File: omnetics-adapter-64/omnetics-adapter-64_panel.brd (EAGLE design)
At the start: 109 x 119 mm, 255 parts, among them J1 DF40-REC, J10 DF40-REC, J13 DF40-REC, J16 DF40-REC, J17 DF40-REC, J22 DF40-REC, J25 DF40-REC, J28 DF40-REC, J31 DF40-REC, J34 DF40-REC, J37 DF40-REC, J4 DF40-REC, J40 DF40-REC, J43 DF40-REC, J46 DF40-REC, J49 DF40-REC, J52 DF40-REC, J55 DF40-REC, J58 DF40-REC, J61 DF40-REC, J64 DF40-REC, J67 DF40-REC, J7 DF40-REC, J70 DF40-REC, J73 DF40-REC, J76 DF40-REC, J79 DF40-REC, J82 DF40-REC

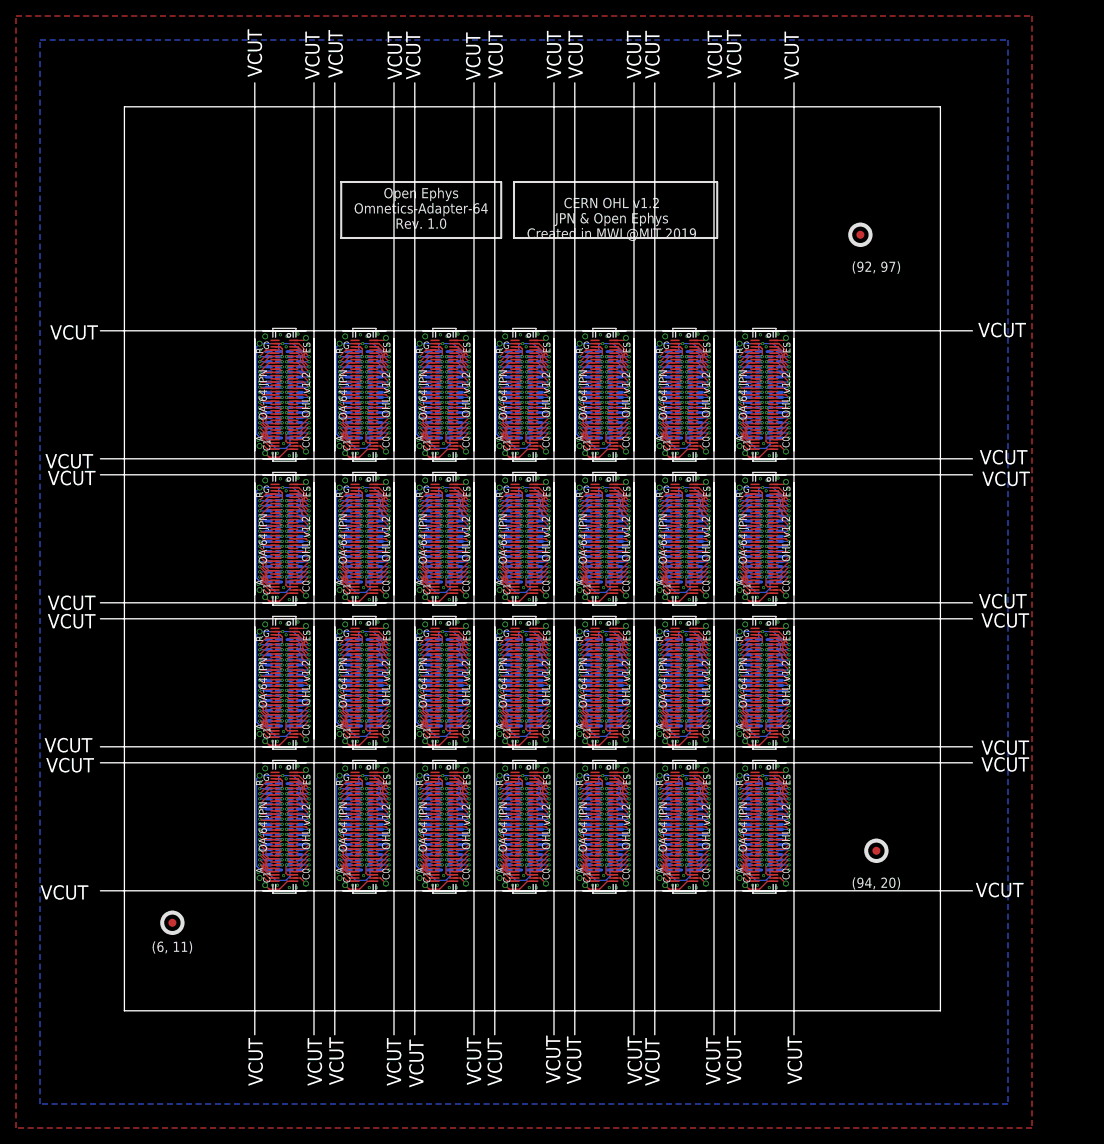
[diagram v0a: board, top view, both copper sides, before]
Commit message: Update omnetics-adapter-64 with Filipe's suggestions
- The suggestions addressed are as follows:
- Increase alls pads of J1 by at least 0.5 mm to the exterior. I believe
this board will be completely assembled by hand and this facilitates
assembly and shorts removal.
- Have 2 mm from the tip of the Omnetics pad to the outline of the
board. This gives us room to apply the necessary epoxy.
- Add some 0.3 holes around the Omnetics to help to fix the epoxy.
- Reduce a little bit the roundness of the Omnetics pads, but not
completely. I would say to half of the current roundness.
- Move the silk indications away from the epoxy application and the
extension of the J1 pads. (done in the board i'm sending)
- Can we write Open-Ephys somewhere in the top silk?
- In the panel, Vcut only for the sides of the board parallel to the
connectors. Milling in the rest. Easier to detach due to J1 being
outside the board boundaries.
- In the panel, a distance between board center to board center of 25 mm
is suggested. (I'm sending the current panel for reference)
- In the panel, if the non-90degrees individual board's corner can
prevail, it would be better: it's more elegant and to grab-friendly.
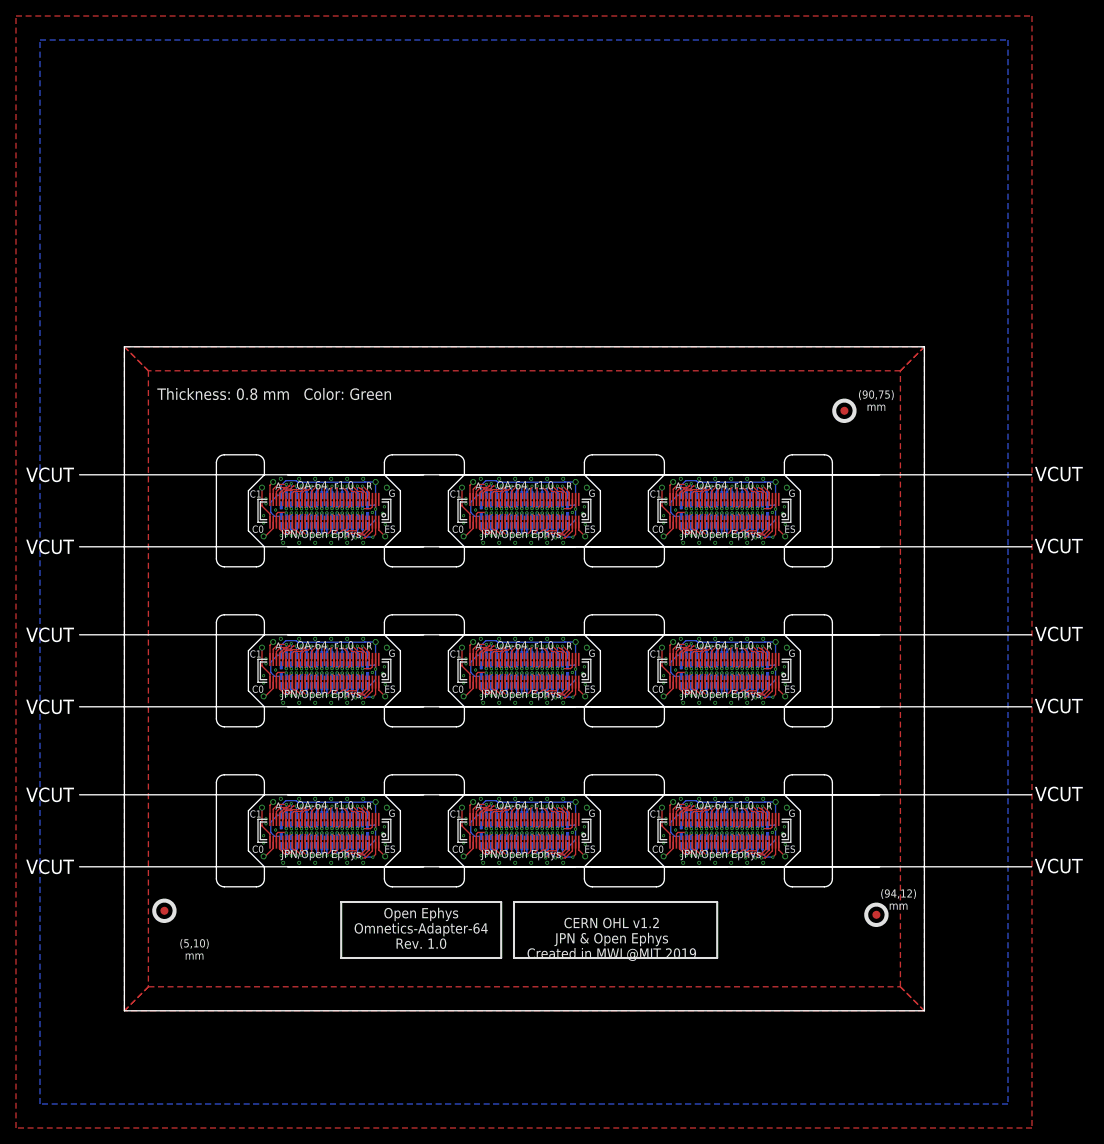
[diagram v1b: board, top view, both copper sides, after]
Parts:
- removed AN10, AN11, AN12, AN13, AN14, AN15, AN16, AN17, AN18, AN19, AN20, AN21, AN22, AN23, AN24, AN25, AN26, AN27, AN28, AN9, CAT18, CAT19, CAT20, CAT21, CAT22, CAT23, CAT24, CAT25, CAT26, CAT27, CAT28, CAT29, CAT30, CAT31, CAT32, CAT33, CAT34, CAT35, CAT36, CAT37, CAT38, CAT39, CAT40, CAT41, CAT42, CAT43, CAT44, CAT45, CAT46, CAT47, CAT48, CAT49, CAT50, CAT51, CAT52, CAT53, CAT54, CAT55, CAT56, ESTIM27, ESTIM28, ESTIM29, ESTIM30, ESTIM31, ESTIM32, ESTIM33, ESTIM34, ESTIM35, ESTIM36, ESTIM37, ESTIM38, ESTIM39, ESTIM40, ESTIM41, ESTIM42, ESTIM43, ESTIM44, ESTIM45, ESTIM46, ESTIM47, ESTIM48, ESTIM49, ESTIM50, ESTIM51, ESTIM52, ESTIM53, ESTIM54, ESTIM55, ESTIM56, ESTIM57, ESTIM58, ESTIM59, ESTIM60, ESTIM61, ESTIM62, ESTIM63, ESTIM64, ESTIM65, ESTIM66, ESTIM67, ESTIM68, ESTIM69, ESTIM70, ESTIM71, ESTIM72, ESTIM73, ESTIM74, ESTIM75, ESTIM76, ESTIM77, ESTIM78, ESTIM79, ESTIM80, ESTIM81, ESTIM82, ESTIM83, ESTIM84: LRG_GP, jonnew:GOLDPIN_0.5ID_0.7OD
- removed E$4: (no value), fiducial:FIDUCIAL
- removed J28, J31, J34, J37, J40, J43, J46, J49, J52, J55, J58, J61, J64, J67, J70, J73, J76, J79, J82: DF40-REC, jonnew:DF40-70REC
- removed J29, J30, J32, J33, J35, J36, J38, J39, J41, J42, J44, J45, J47, J48, J50, J51, J53, J54, J56, J57, J59, J60, J62, J63, J65, J66, J68, J69, J71, J72, J74, J75, J77, J78, J80, J81, J83, J84: (no value), jonnew:NPD-36-VV-GS
- added AN, CAT0, ESTIM: LRG_GP, jonnew:GOLDPIN_0.5ID_0.7OD
- added E$3: (no value), fiducial:FIDUCIAL
- J1, J10, J13, J16, J22, J25, J4, J7: device jonnew:DF40-70REC -> jonnew:DDF40-70REC-LRG
- J17: value DF40-REC -> (none); device jonnew:DF40-70REC -> jonnew:NPD-36-VV-GS
- J19: value (none) -> DF40-REC; device jonnew:NPD-36-VV-GS -> jonnew:DDF40-70REC-LRG
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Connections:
- removed net AN10: AN10.P$1, J31.36
- removed net AN11: AN11.P$1, J34.36
- removed net AN12: AN12.P$1, J37.36
- removed net AN13: AN13.P$1, J40.36
- removed net AN14: AN14.P$1, J43.36
- removed net AN15: AN15.P$1, J46.36
- removed net AN16: AN16.P$1, J17.36
- removed net AN17: AN17.P$1, J49.36
- removed net AN18: AN18.P$1, J52.36
- removed net AN19: AN19.P$1, J55.36
- removed net AN20: AN20.P$1, J58.36
- removed net AN21: AN21.P$1, J61.36
- removed net AN22: AN22.P$1, J64.36
- removed net AN23: AN23.P$1, J67.36
- removed net AN24: AN24.P$1, J70.36
- removed net AN25: AN25.P$1, J73.36
- removed net AN26: AN26.P$1, J76.36
- removed net AN27: AN27.P$1, J79.36
- removed net AN28: AN28.P$1, J82.36
- removed net AN9: AN9.P$1, J28.36
- removed net CAT18: CAT18.P$1, J28.35
- removed net CAT19: CAT19.P$1, J31.34
- removed net CAT20: CAT20.P$1, J31.35
- removed net CAT21: CAT21.P$1, J34.34
- removed net CAT22: CAT22.P$1, J34.35
- removed net CAT23: CAT23.P$1, J37.34
- removed net CAT24: CAT24.P$1, J37.35
- removed net CAT25: CAT25.P$1, J40.34
- removed net CAT26: CAT26.P$1, J40.35
- removed net CAT27: CAT27.P$1, J43.34
- removed net CAT28: CAT28.P$1, J43.35
- removed net CAT29: CAT29.P$1, J46.34
- removed net CAT30: CAT30.P$1, J46.35
- removed net CAT31: CAT31.P$1, J49.34
- removed net CAT32: CAT32.P$1, J17.34
- removed net CAT33: CAT33.P$1, J17.35
- removed net CAT34: CAT34.P$1, J49.35
- removed net CAT35: CAT35.P$1, J52.34
- removed net CAT36: CAT36.P$1, J52.35
- removed net CAT37: CAT37.P$1, J55.34
- removed net CAT38: CAT38.P$1, J55.35
- removed net CAT39: CAT39.P$1, J58.34
- removed net CAT40: CAT40.P$1, J58.35
- removed net CAT41: CAT41.P$1, J61.34
- removed net CAT42: CAT42.P$1, J61.35
- removed net CAT43: CAT43.P$1, J64.34
- removed net CAT44: CAT44.P$1, J64.35
- removed net CAT45: CAT45.P$1, J67.34
- removed net CAT46: CAT46.P$1, J67.35
- removed net CAT47: CAT47.P$1, J70.34
- removed net CAT48: CAT48.P$1, J70.35
- removed net CAT49: CAT49.P$1, J73.34
- removed net CAT50: CAT50.P$1, J73.35
- removed net CAT51: CAT51.P$1, J76.34
- removed net CAT52: CAT52.P$1, J76.35
- removed net CAT53: CAT53.P$1, J79.34
- removed net CAT54: CAT54.P$1, J79.35
- removed net CAT55: CAT55.P$1, J82.34
- removed net CAT56: CAT56.P$1, J82.35
- removed net ESTIM10: ESTIM31.P$1, J31.1
- removed net ESTIM11: ESTIM34.P$1, J34.1
- removed net ESTIM12: ESTIM37.P$1, J37.1
- removed net ESTIM13: ESTIM40.P$1, J40.1
- removed net ESTIM14: ESTIM43.P$1, J43.1
- removed net ESTIM15: ESTIM46.P$1, J46.1
- removed net ESTIM16: ESTIM16.P$1, J17.1
- removed net ESTIM17: ESTIM49.P$1, J49.1
- removed net ESTIM18: ESTIM52.P$1, J52.1
- removed net ESTIM19: ESTIM55.P$1, J55.1
- removed net ESTIM20: ESTIM58.P$1, J58.1
- removed net ESTIM21: ESTIM61.P$1, J61.1
- removed net ESTIM22: ESTIM64.P$1, J64.1
- removed net ESTIM23: ESTIM67.P$1, J67.1
- removed net ESTIM24: ESTIM70.P$1, J70.1
- removed net ESTIM25: ESTIM73.P$1, J73.1
- removed net ESTIM26: ESTIM76.P$1, J76.1
- removed net ESTIM27: ESTIM79.P$1, J79.1
- removed net ESTIM28: ESTIM82.P$1, J82.1
- removed net ESTIM9: ESTIM28.P$1, J28.1
- removed net N$1000: J49.54, J50.27
- removed net N$1001: J49.53, J50.10
- removed net N$1002: J49.52, J50.28
- removed net N$1003: J49.51, J50.9
- removed net N$1004: J49.50, J50.29
- removed net N$1005: J49.49, J50.8
- removed net N$1006: J49.48, J50.30
- removed net N$1007: J49.47, J50.31
- removed net N$1008: J49.46, J50.7
- removed net N$1009: J49.45, J50.32
- removed net N$1010: J49.44, J50.33
- removed net N$1011: J49.43, J50.6
- removed net N$1012: J49.42, J50.34
- removed net N$1013: J49.41, J50.35
- removed net N$1014: J49.40, J50.5
- removed net N$1015: J49.38, J50.3
- removed net N$1016: J49.5, J51.23
- removed net N$1017: J49.4, J51.22
- removed net N$1018: J49.3, J51.21
- removed net N$1019: J49.2, J51.20
- removed net N$1020: J49.65, J50.15
- removed net N$1021: J49.67, J50.17
- removed net N$1022: J49.39, J50.4
- removed net N$1023: J49.37, J50.2
- removed net N$1024: J49.33, J51.2
- removed net N$1025: J17.32, J19.35
- removed net N$1026: J17.31, J19.34
- removed net N$1027: J17.30, J19.33
- removed net N$1028: J17.29, J19.3
- removed net N$1029: J17.28, J19.32
- removed net N$1030: J17.27, J19.4
- removed net N$1031: J17.26, J19.5
- removed net N$1032: J17.25, J19.31
- removed net N$1033: J17.24, J19.6
- removed net N$1034: J17.23, J19.7
- removed net N$1035: J17.22, J19.30
- removed net N$1036: J17.21, J19.8
- removed net N$1037: J17.20, J19.29
- removed net N$1038: J17.19, J19.9
- removed net N$1039: J17.18, J19.28
- removed net N$1040: J17.17, J19.10
- removed net N$1041: J17.16, J19.27
- removed net N$1042: J17.15, J19.11
- removed net N$1043: J17.14, J19.26
- removed net N$1044: J17.13, J19.12
- removed net N$1045: J17.12, J19.13
- removed net N$1046: J17.11, J19.25
- removed net N$1047: J17.10, J19.14
- removed net N$1048: J17.9, J19.15
- removed net N$1049: J17.8, J19.24
- removed net N$1050: J17.7, J19.16
- removed net N$1051: J17.6, J19.17
- removed net N$1052: J17.68, J18.20
- removed net N$1053: J17.66, J18.16
- removed net N$1054: J17.64, J18.21
- removed net N$1055: J17.63, J18.14
- removed net N$1056: J17.62, J18.22
- removed net N$1057: J17.61, J18.23
- removed net N$1058: J17.60, J18.13
- removed net N$1059: J17.59, J18.24
- removed net N$1060: J17.58, J18.25
- removed net N$1061: J17.57, J18.12
- removed net N$1062: J17.56, J18.26
- removed net N$1063: J17.55, J18.11
- removed net N$1064: J17.54, J18.27
- removed net N$1065: J17.53, J18.10
- removed net N$1066: J17.52, J18.28
- removed net N$1067: J17.51, J18.9
- removed net N$1068: J17.50, J18.29
- removed net N$1069: J17.49, J18.8
- removed net N$1070: J17.48, J18.30
- removed net N$1071: J17.47, J18.31
- removed net N$1072: J17.46, J18.7
- removed net N$1073: J17.45, J18.32
- removed net N$1074: J17.44, J18.33
- removed net N$1075: J17.43, J18.6
- removed net N$1076: J17.42, J18.34
- removed net N$1077: J17.41, J18.35
- removed net N$1078: J17.40, J18.5
- removed net N$1079: J17.38, J18.3
- removed net N$1080: J17.5, J19.23
- removed net N$1081: J17.4, J19.22
- removed net N$1082: J17.3, J19.21
- removed net N$1083: J17.2, J19.20
- removed net N$1084: J17.65, J18.15
- removed net N$1085: J17.67, J18.17
- removed net N$1086: J17.39, J18.4
- removed net N$1087: J17.37, J18.2
- removed net N$1088: J17.33, J19.2
- removed net N$1089: J52.32, J54.35
- removed net N$1090: J52.31, J54.34
- removed net N$1091: J52.30, J54.33
- removed net N$1092: J52.29, J54.3
- removed net N$1093: J52.28, J54.32
- removed net N$1094: J52.27, J54.4
- removed net N$1095: J52.26, J54.5
- removed net N$1096: J52.25, J54.31
- removed net N$1097: J52.24, J54.6
- removed net N$1098: J52.23, J54.7
- removed net N$1099: J52.22, J54.30
- removed net N$1100: J52.21, J54.8
- removed net N$1101: J52.20, J54.29
- removed net N$1102: J52.19, J54.9
- removed net N$1103: J52.18, J54.28
- removed net N$1104: J52.17, J54.10
- removed net N$1105: J52.16, J54.27
- removed net N$1106: J52.15, J54.11
- removed net N$1107: J52.14, J54.26
- removed net N$1108: J52.13, J54.12
- removed net N$1109: J52.12, J54.13
- removed net N$1110: J52.11, J54.25
- removed net N$1111: J52.10, J54.14
- removed net N$1112: J52.9, J54.15
- removed net N$1113: J52.8, J54.24
- removed net N$1114: J52.7, J54.16
- removed net N$1115: J52.6, J54.17
- removed net N$1116: J52.68, J53.20
- removed net N$1117: J52.66, J53.16
- removed net N$1118: J52.64, J53.21
- removed net N$1119: J52.63, J53.14
- removed net N$1120: J52.62, J53.22
- removed net N$1121: J52.61, J53.23
- removed net N$1122: J52.60, J53.13
- removed net N$1123: J52.59, J53.24
- removed net N$1124: J52.58, J53.25
- removed net N$1125: J52.57, J53.12
- removed net N$1126: J52.56, J53.26
- removed net N$1127: J52.55, J53.11
- removed net N$1128: J52.54, J53.27
- removed net N$1129: J52.53, J53.10
- removed net N$1130: J52.52, J53.28
- removed net N$1131: J52.51, J53.9
- removed net N$1132: J52.50, J53.29
- removed net N$1133: J52.49, J53.8
- removed net N$1134: J52.48, J53.30
- removed net N$1135: J52.47, J53.31
- removed net N$1136: J52.46, J53.7
- removed net N$1137: J52.45, J53.32
- removed net N$1138: J52.44, J53.33
- removed net N$1139: J52.43, J53.6
- removed net N$1140: J52.42, J53.34
- removed net N$1141: J52.41, J53.35
- removed net N$1142: J52.40, J53.5
- removed net N$1143: J52.38, J53.3
- removed net N$1144: J52.5, J54.23
- removed net N$1145: J52.4, J54.22
- removed net N$1146: J52.3, J54.21
- removed net N$1147: J52.2, J54.20
- removed net N$1148: J52.65, J53.15
- removed net N$1149: J52.67, J53.17
- removed net N$1150: J52.39, J53.4
- removed net N$1151: J52.37, J53.2
- removed net N$1152: J52.33, J54.2
- removed net N$1153: J55.32, J57.35
- removed net N$1154: J55.31, J57.34
- removed net N$1155: J55.30, J57.33
- removed net N$1156: J55.29, J57.3
- removed net N$1157: J55.28, J57.32
- removed net N$1158: J55.27, J57.4
- removed net N$1159: J55.26, J57.5
- removed net N$1160: J55.25, J57.31
- removed net N$1161: J55.24, J57.6
- removed net N$1162: J55.23, J57.7
- removed net N$1163: J55.22, J57.30
- removed net N$1164: J55.21, J57.8
- removed net N$1165: J55.20, J57.29
- removed net N$1166: J55.19, J57.9
- removed net N$1167: J55.18, J57.28
- removed net N$1168: J55.17, J57.10
- removed net N$1169: J55.16, J57.27
- removed net N$1170: J55.15, J57.11
- removed net N$1171: J55.14, J57.26
- removed net N$1172: J55.13, J57.12
- removed net N$1173: J55.12, J57.13
- removed net N$1174: J55.11, J57.25
- removed net N$1175: J55.10, J57.14
- removed net N$1176: J55.9, J57.15
- removed net N$1177: J55.8, J57.24
- removed net N$1178: J55.7, J57.16
- removed net N$1179: J55.6, J57.17
- removed net N$1180: J55.68, J56.20
- removed net N$1181: J55.66, J56.16
- removed net N$1182: J55.64, J56.21
- removed net N$1183: J55.63, J56.14
- removed net N$1184: J55.62, J56.22
- removed net N$1185: J55.61, J56.23
- removed net N$1186: J55.60, J56.13
- removed net N$1187: J55.59, J56.24
- removed net N$1188: J55.58, J56.25
- removed net N$1189: J55.57, J56.12
- removed net N$1190: J55.56, J56.26
- removed net N$1191: J55.55, J56.11
- removed net N$1192: J55.54, J56.27
- removed net N$1193: J55.53, J56.10
- removed net N$1194: J55.52, J56.28
- removed net N$1195: J55.51, J56.9
- removed net N$1196: J55.50, J56.29
- removed net N$1197: J55.49, J56.8
- removed net N$1198: J55.48, J56.30
- removed net N$1199: J55.47, J56.31
- removed net N$1200: J55.46, J56.7
- removed net N$1201: J55.45, J56.32
- removed net N$1202: J55.44, J56.33
- removed net N$1203: J55.43, J56.6
- removed net N$1204: J55.42, J56.34
- removed net N$1205: J55.41, J56.35
- removed net N$1206: J55.40, J56.5
- removed net N$1207: J55.38, J56.3
- removed net N$1208: J55.5, J57.23
- removed net N$1209: J55.4, J57.22
- removed net N$1210: J55.3, J57.21
- removed net N$1211: J55.2, J57.20
- removed net N$1212: J55.65, J56.15
- removed net N$1213: J55.67, J56.17
- removed net N$1214: J55.39, J56.4
- removed net N$1215: J55.37, J56.2
- removed net N$1216: J55.33, J57.2
- removed net N$1217: J58.32, J60.35
- removed net N$1218: J58.31, J60.34
- removed net N$1219: J58.30, J60.33
- removed net N$1220: J58.29, J60.3
- removed net N$1221: J58.28, J60.32
- removed net N$1222: J58.27, J60.4
- removed net N$1223: J58.26, J60.5
- removed net N$1224: J58.25, J60.31
- removed net N$1225: J58.24, J60.6
- removed net N$1226: J58.23, J60.7
- removed net N$1227: J58.22, J60.30
- removed net N$1228: J58.21, J60.8
- removed net N$1229: J58.20, J60.29
- removed net N$1230: J58.19, J60.9
- removed net N$1231: J58.18, J60.28
- removed net N$1232: J58.17, J60.10
- removed net N$1233: J58.16, J60.27
- removed net N$1234: J58.15, J60.11
- removed net N$1235: J58.14, J60.26
- removed net N$1236: J58.13, J60.12
- removed net N$1237: J58.12, J60.13
- removed net N$1238: J58.11, J60.25
- removed net N$1239: J58.10, J60.14
- removed net N$1240: J58.9, J60.15
- removed net N$1241: J58.8, J60.24
- removed net N$1242: J58.7, J60.16
- removed net N$1243: J58.6, J60.17
- removed net N$1244: J58.68, J59.20
- removed net N$1245: J58.66, J59.16
- removed net N$1246: J58.64, J59.21
- removed net N$1247: J58.63, J59.14
- removed net N$1248: J58.62, J59.22
- removed net N$1249: J58.61, J59.23
- removed net N$1250: J58.60, J59.13
- removed net N$1251: J58.59, J59.24
- removed net N$1252: J58.58, J59.25
- removed net N$1253: J58.57, J59.12
- removed net N$1254: J58.56, J59.26
- removed net N$1255: J58.55, J59.11
- removed net N$1256: J58.54, J59.27
- removed net N$1257: J58.53, J59.10
- removed net N$1258: J58.52, J59.28
- removed net N$1259: J58.51, J59.9
- removed net N$1260: J58.50, J59.29
- removed net N$1261: J58.49, J59.8
- removed net N$1262: J58.48, J59.30
- removed net N$1263: J58.47, J59.31
- removed net N$1264: J58.46, J59.7
- removed net N$1265: J58.45, J59.32
- removed net N$1266: J58.44, J59.33
- removed net N$1267: J58.43, J59.6
- removed net N$1268: J58.42, J59.34
- removed net N$1269: J58.41, J59.35
- removed net N$1270: J58.40, J59.5
- removed net N$1271: J58.38, J59.3
- removed net N$1272: J58.5, J60.23
- removed net N$1273: J58.4, J60.22
- removed net N$1274: J58.3, J60.21
- removed net N$1275: J58.2, J60.20
- removed net N$1276: J58.65, J59.15
- removed net N$1277: J58.67, J59.17
- removed net N$1278: J58.39, J59.4
- removed net N$1279: J58.37, J59.2
- removed net N$1280: J58.33, J60.2
- removed net N$1281: J61.32, J63.35
- removed net N$1282: J61.31, J63.34
- removed net N$1283: J61.30, J63.33
- removed net N$1284: J61.29, J63.3
- removed net N$1285: J61.28, J63.32
- removed net N$1286: J61.27, J63.4
- removed net N$1287: J61.26, J63.5
- removed net N$1288: J61.25, J63.31
- removed net N$1289: J61.24, J63.6
- removed net N$1290: J61.23, J63.7
- removed net N$1291: J61.22, J63.30
- removed net N$1292: J61.21, J63.8
- removed net N$1293: J61.20, J63.29
- removed net N$1294: J61.19, J63.9
- removed net N$1295: J61.18, J63.28
- removed net N$1296: J61.17, J63.10
- removed net N$1297: J61.16, J63.27
- removed net N$1298: J61.15, J63.11
- removed net N$1299: J61.14, J63.26
- removed net N$1300: J61.13, J63.12
- removed net N$1301: J61.12, J63.13
- removed net N$1302: J61.11, J63.25
- removed net N$1303: J61.10, J63.14
- removed net N$1304: J61.9, J63.15
- removed net N$1305: J61.8, J63.24
- removed net N$1306: J61.7, J63.16
- removed net N$1307: J61.6, J63.17
- removed net N$1308: J61.68, J62.20
- removed net N$1309: J61.66, J62.16
- removed net N$1310: J61.64, J62.21
- removed net N$1311: J61.63, J62.14
- removed net N$1312: J61.62, J62.22
- removed net N$1313: J61.61, J62.23
- removed net N$1314: J61.60, J62.13
- removed net N$1315: J61.59, J62.24
- removed net N$1316: J61.58, J62.25
- removed net N$1317: J61.57, J62.12
- removed net N$1318: J61.56, J62.26
- removed net N$1319: J61.55, J62.11
- removed net N$1320: J61.54, J62.27
- removed net N$1321: J61.53, J62.10
- removed net N$1322: J61.52, J62.28
- removed net N$1323: J61.51, J62.9
- removed net N$1324: J61.50, J62.29
- removed net N$1325: J61.49, J62.8
- removed net N$1326: J61.48, J62.30
- removed net N$1327: J61.47, J62.31
- removed net N$1328: J61.46, J62.7
- removed net N$1329: J61.45, J62.32
- removed net N$1330: J61.44, J62.33
- removed net N$1331: J61.43, J62.6
- removed net N$1332: J61.42, J62.34
- removed net N$1333: J61.41, J62.35
- removed net N$1334: J61.40, J62.5
- removed net N$1335: J61.38, J62.3
- removed net N$1336: J61.5, J63.23
- removed net N$1337: J61.4, J63.22
- removed net N$1338: J61.3, J63.21
- removed net N$1339: J61.2, J63.20
- removed net N$1340: J61.65, J62.15
- removed net N$1341: J61.67, J62.17
- removed net N$1342: J61.39, J62.4
- removed net N$1343: J61.37, J62.2
- removed net N$1344: J61.33, J63.2
- removed net N$1345: J64.32, J66.35
- removed net N$1346: J64.31, J66.34
- removed net N$1347: J64.30, J66.33
- removed net N$1348: J64.29, J66.3
- removed net N$1349: J64.28, J66.32
- removed net N$1350: J64.27, J66.4
- removed net N$1351: J64.26, J66.5
- removed net N$1352: J64.25, J66.31
- removed net N$1353: J64.24, J66.6
- removed net N$1354: J64.23, J66.7
- removed net N$1355: J64.22, J66.30
- removed net N$1356: J64.21, J66.8
- removed net N$1357: J64.20, J66.29
- removed net N$1358: J64.19, J66.9
- removed net N$1359: J64.18, J66.28
- removed net N$1360: J64.17, J66.10
- removed net N$1361: J64.16, J66.27
- removed net N$1362: J64.15, J66.11
- removed net N$1363: J64.14, J66.26
- removed net N$1364: J64.13, J66.12
- removed net N$1365: J64.12, J66.13
- removed net N$1366: J64.11, J66.25
- removed net N$1367: J64.10, J66.14
- removed net N$1368: J64.9, J66.15
- removed net N$1369: J64.8, J66.24
- removed net N$1370: J64.7, J66.16
- removed net N$1371: J64.6, J66.17
- removed net N$1372: J64.68, J65.20
- removed net N$1373: J64.66, J65.16
- removed net N$1374: J64.64, J65.21
- removed net N$1375: J64.63, J65.14
- removed net N$1376: J64.62, J65.22
- removed net N$1377: J64.61, J65.23
- removed net N$1378: J64.60, J65.13
- removed net N$1379: J64.59, J65.24
- removed net N$1380: J64.58, J65.25
- removed net N$1381: J64.57, J65.12
- removed net N$1382: J64.56, J65.26
- removed net N$1383: J64.55, J65.11
- removed net N$1384: J64.54, J65.27
- removed net N$1385: J64.53, J65.10
- removed net N$1386: J64.52, J65.28
- removed net N$1387: J64.51, J65.9
- removed net N$1388: J64.50, J65.29
- removed net N$1389: J64.49, J65.8
- removed net N$1390: J64.48, J65.30
- removed net N$1391: J64.47, J65.31
- removed net N$1392: J64.46, J65.7
- removed net N$1393: J64.45, J65.32
- removed net N$1394: J64.44, J65.33
- removed net N$1395: J64.43, J65.6
- removed net N$1396: J64.42, J65.34
- removed net N$1397: J64.41, J65.35
- removed net N$1398: J64.40, J65.5
- removed net N$1399: J64.38, J65.3
- removed net N$1400: J64.5, J66.23
- removed net N$1401: J64.4, J66.22
- removed net N$1402: J64.3, J66.21
- removed net N$1403: J64.2, J66.20
- removed net N$1404: J64.65, J65.15
- removed net N$1405: J64.67, J65.17
- removed net N$1406: J64.39, J65.4
- removed net N$1407: J64.37, J65.2
- removed net N$1408: J64.33, J66.2
- removed net N$1409: J67.32, J69.35
- removed net N$1410: J67.31, J69.34
- removed net N$1411: J67.30, J69.33
- removed net N$1412: J67.29, J69.3
- removed net N$1413: J67.28, J69.32
- removed net N$1414: J67.27, J69.4
- removed net N$1415: J67.26, J69.5
- removed net N$1416: J67.25, J69.31
- removed net N$1417: J67.24, J69.6
- removed net N$1418: J67.23, J69.7
- removed net N$1419: J67.22, J69.30
- removed net N$1420: J67.21, J69.8
- removed net N$1421: J67.20, J69.29
- removed net N$1422: J67.19, J69.9
- removed net N$1423: J67.18, J69.28
- removed net N$1424: J67.17, J69.10
- removed net N$1425: J67.16, J69.27
- removed net N$1426: J67.15, J69.11
- removed net N$1427: J67.14, J69.26
- removed net N$1428: J67.13, J69.12
- removed net N$1429: J67.12, J69.13
- removed net N$1430: J67.11, J69.25
- removed net N$1431: J67.10, J69.14
- removed net N$1432: J67.9, J69.15
- removed net N$1433: J67.8, J69.24
- removed net N$1434: J67.7, J69.16
- removed net N$1435: J67.6, J69.17
- removed net N$1436: J67.68, J68.20
- removed net N$1437: J67.66, J68.16
- removed net N$1438: J67.64, J68.21
- removed net N$1439: J67.63, J68.14
- removed net N$1440: J67.62, J68.22
- removed net N$1441: J67.61, J68.23
- removed net N$1442: J67.60, J68.13
- removed net N$1443: J67.59, J68.24
- removed net N$1444: J67.58, J68.25
- removed net N$1445: J67.57, J68.12
- removed net N$1446: J67.56, J68.26
- removed net N$1447: J67.55, J68.11
- removed net N$1448: J67.54, J68.27
- removed net N$1449: J67.53, J68.10
- removed net N$1450: J67.52, J68.28
- removed net N$1451: J67.51, J68.9
- removed net N$1452: J67.50, J68.29
- removed net N$1453: J67.49, J68.8
- removed net N$1454: J67.48, J68.30
- removed net N$1455: J67.47, J68.31
- removed net N$1456: J67.46, J68.7
- removed net N$1457: J67.45, J68.32
- removed net N$1458: J67.44, J68.33
- removed net N$1459: J67.43, J68.6
- removed net N$1460: J67.42, J68.34
- removed net N$1461: J67.41, J68.35
- removed net N$1462: J67.40, J68.5
- removed net N$1463: J67.38, J68.3
- removed net N$1464: J67.5, J69.23
- removed net N$1465: J67.4, J69.22
- removed net N$1466: J67.3, J69.21
- removed net N$1467: J67.2, J69.20
- removed net N$1468: J67.65, J68.15
- removed net N$1469: J67.67, J68.17
- removed net N$1470: J67.39, J68.4
- removed net N$1471: J67.37, J68.2
- removed net N$1472: J67.33, J69.2
- removed net N$1473: J70.32, J72.35
- removed net N$1474: J70.31, J72.34
- removed net N$1475: J70.30, J72.33
- removed net N$1476: J70.29, J72.3
- removed net N$1477: J70.28, J72.32
- removed net N$1478: J70.27, J72.4
- removed net N$1479: J70.26, J72.5
- removed net N$1480: J70.25, J72.31
- removed net N$1481: J70.24, J72.6
- removed net N$1482: J70.23, J72.7
- removed net N$1483: J70.22, J72.30
- removed net N$1484: J70.21, J72.8
- removed net N$1485: J70.20, J72.29
- removed net N$1486: J70.19, J72.9
- removed net N$1487: J70.18, J72.28
- removed net N$1488: J70.17, J72.10
- removed net N$1489: J70.16, J72.27
- removed net N$1490: J70.15, J72.11
- removed net N$1491: J70.14, J72.26
- removed net N$1492: J70.13, J72.12
- removed net N$1493: J70.12, J72.13
- removed net N$1494: J70.11, J72.25
- removed net N$1495: J70.10, J72.14
- removed net N$1496: J70.9, J72.15
- removed net N$1497: J70.8, J72.24
- removed net N$1498: J70.7, J72.16
- removed net N$1499: J70.6, J72.17
- removed net N$1500: J70.68, J71.20
- removed net N$1501: J70.66, J71.16
- removed net N$1502: J70.64, J71.21
- removed net N$1503: J70.63, J71.14
- removed net N$1504: J70.62, J71.22
- removed net N$1505: J70.61, J71.23
- removed net N$1506: J70.60, J71.13
- removed net N$1507: J70.59, J71.24
- removed net N$1508: J70.58, J71.25
- removed net N$1509: J70.57, J71.12
- removed net N$1510: J70.56, J71.26
- removed net N$1511: J70.55, J71.11
- removed net N$1512: J70.54, J71.27
- removed net N$1513: J70.53, J71.10
- removed net N$1514: J70.52, J71.28
- removed net N$1515: J70.51, J71.9
- removed net N$1516: J70.50, J71.29
- removed net N$1517: J70.49, J71.8
- removed net N$1518: J70.48, J71.30
- removed net N$1519: J70.47, J71.31
- removed net N$1520: J70.46, J71.7
- removed net N$1521: J70.45, J71.32
- removed net N$1522: J70.44, J71.33
- removed net N$1523: J70.43, J71.6
- removed net N$1524: J70.42, J71.34
- removed net N$1525: J70.41, J71.35
- removed net N$1526: J70.40, J71.5
- removed net N$1527: J70.38, J71.3
- removed net N$1528: J70.5, J72.23
- removed net N$1529: J70.4, J72.22
- removed net N$1530: J70.3, J72.21
- removed net N$1531: J70.2, J72.20
- removed net N$1532: J70.65, J71.15
- removed net N$1533: J70.67, J71.17
- removed net N$1534: J70.39, J71.4
- removed net N$1535: J70.37, J71.2
- removed net N$1536: J70.33, J72.2
- removed net N$1537: J73.32, J75.35
- removed net N$1538: J73.31, J75.34
- removed net N$1539: J73.30, J75.33
- removed net N$1540: J73.29, J75.3
- removed net N$1541: J73.28, J75.32
- removed net N$1542: J73.27, J75.4
- removed net N$1543: J73.26, J75.5
- removed net N$1544: J73.25, J75.31
- removed net N$1545: J73.24, J75.6
- removed net N$1546: J73.23, J75.7
- removed net N$1547: J73.22, J75.30
- removed net N$1548: J73.21, J75.8
- removed net N$1549: J73.20, J75.29
- removed net N$1550: J73.19, J75.9
- removed net N$1551: J73.18, J75.28
- removed net N$1552: J73.17, J75.10
- removed net N$1553: J73.16, J75.27
- removed net N$1554: J73.15, J75.11
- removed net N$1555: J73.14, J75.26
- removed net N$1556: J73.13, J75.12
- removed net N$1557: J73.12, J75.13
- removed net N$1558: J73.11, J75.25
- removed net N$1559: J73.10, J75.14
- removed net N$1560: J73.9, J75.15
- removed net N$1561: J73.8, J75.24
- removed net N$1562: J73.7, J75.16
- removed net N$1563: J73.6, J75.17
- removed net N$1564: J73.68, J74.20
- removed net N$1565: J73.66, J74.16
- removed net N$1566: J73.64, J74.21
- removed net N$1567: J73.63, J74.14
- removed net N$1568: J73.62, J74.22
- removed net N$1569: J73.61, J74.23
- removed net N$1570: J73.60, J74.13
- removed net N$1571: J73.59, J74.24
- removed net N$1572: J73.58, J74.25
- removed net N$1573: J73.57, J74.12
- removed net N$1574: J73.56, J74.26
- removed net N$1575: J73.55, J74.11
- removed net N$1576: J73.54, J74.27
- removed net N$1577: J73.53, J74.10
- removed net N$1578: J73.52, J74.28
- removed net N$1579: J73.51, J74.9
- removed net N$1580: J73.50, J74.29
- removed net N$1581: J73.49, J74.8
- removed net N$1582: J73.48, J74.30
- removed net N$1583: J73.47, J74.31
- removed net N$1584: J73.46, J74.7
- removed net N$1585: J73.45, J74.32
- removed net N$1586: J73.44, J74.33
- removed net N$1587: J73.43, J74.6
- removed net N$1588: J73.42, J74.34
- removed net N$1589: J73.41, J74.35
- removed net N$1590: J73.40, J74.5
- removed net N$1591: J73.38, J74.3
- removed net N$1592: J73.5, J75.23
- removed net N$1593: J73.4, J75.22
- removed net N$1594: J73.3, J75.21
- removed net N$1595: J73.2, J75.20
- removed net N$1596: J73.65, J74.15
- removed net N$1597: J73.67, J74.17
- removed net N$1598: J73.39, J74.4
- removed net N$1599: J73.37, J74.2
- removed net N$1600: J73.33, J75.2
- removed net N$1601: J76.32, J78.35
- removed net N$1602: J76.31, J78.34
- removed net N$1603: J76.30, J78.33
- removed net N$1604: J76.29, J78.3
- removed net N$1605: J76.28, J78.32
- removed net N$1606: J76.27, J78.4
- removed net N$1607: J76.26, J78.5
- removed net N$1608: J76.25, J78.31
- removed net N$1609: J76.24, J78.6
- removed net N$1610: J76.23, J78.7
- removed net N$1611: J76.22, J78.30
- removed net N$1612: J76.21, J78.8
- removed net N$1613: J76.20, J78.29
- removed net N$1614: J76.19, J78.9
- removed net N$1615: J76.18, J78.28
- removed net N$1616: J76.17, J78.10
- removed net N$1617: J76.16, J78.27
- removed net N$1618: J76.15, J78.11
- removed net N$1619: J76.14, J78.26
- removed net N$1620: J76.13, J78.12
- removed net N$1621: J76.12, J78.13
- removed net N$1622: J76.11, J78.25
- removed net N$1623: J76.10, J78.14
- removed net N$1624: J76.9, J78.15
- removed net N$1625: J76.8, J78.24
- removed net N$1626: J76.7, J78.16
- removed net N$1627: J76.6, J78.17
- removed net N$1628: J76.68, J77.20
- removed net N$1629: J76.66, J77.16
- removed net N$1630: J76.64, J77.21
- removed net N$1631: J76.63, J77.14
- removed net N$1632: J76.62, J77.22
- removed net N$1633: J76.61, J77.23
- removed net N$1634: J76.60, J77.13
- removed net N$1635: J76.59, J77.24
- removed net N$1636: J76.58, J77.25
- removed net N$1637: J76.57, J77.12
- removed net N$1638: J76.56, J77.26
- removed net N$1639: J76.55, J77.11
- removed net N$1640: J76.54, J77.27
- removed net N$1641: J76.53, J77.10
- removed net N$1642: J76.52, J77.28
- removed net N$1643: J76.51, J77.9
- removed net N$1644: J76.50, J77.29
- removed net N$1645: J76.49, J77.8
- removed net N$1646: J76.48, J77.30
- removed net N$1647: J76.47, J77.31
- removed net N$1648: J76.46, J77.7
- removed net N$1649: J76.45, J77.32
- removed net N$1650: J76.44, J77.33
- removed net N$1651: J76.43, J77.6
- removed net N$1652: J76.42, J77.34
- removed net N$1653: J76.41, J77.35
- removed net N$1654: J76.40, J77.5
- removed net N$1655: J76.38, J77.3
- removed net N$1656: J76.5, J78.23
- removed net N$1657: J76.4, J78.22
- removed net N$1658: J76.3, J78.21
- removed net N$1659: J76.2, J78.20
- removed net N$1660: J76.65, J77.15
- removed net N$1661: J76.67, J77.17
- removed net N$1662: J76.39, J77.4
- removed net N$1663: J76.37, J77.2
- removed net N$1664: J76.33, J78.2
- removed net N$1665: J79.32, J81.35
- removed net N$1666: J79.31, J81.34
- removed net N$1667: J79.30, J81.33
- removed net N$1668: J79.29, J81.3
- removed net N$1669: J79.28, J81.32
- removed net N$1670: J79.27, J81.4
- removed net N$1671: J79.26, J81.5
- removed net N$1672: J79.25, J81.31
- removed net N$1673: J79.24, J81.6
- removed net N$1674: J79.23, J81.7
- removed net N$1675: J79.22, J81.30
- removed net N$1676: J79.21, J81.8
- removed net N$1677: J79.20, J81.29
- removed net N$1678: J79.19, J81.9
- removed net N$1679: J79.18, J81.28
- removed net N$1680: J79.17, J81.10
- removed net N$1681: J79.16, J81.27
- removed net N$1682: J79.15, J81.11
- removed net N$1683: J79.14, J81.26
- removed net N$1684: J79.13, J81.12
- removed net N$1685: J79.12, J81.13
- removed net N$1686: J79.11, J81.25
- removed net N$1687: J79.10, J81.14
- removed net N$1688: J79.9, J81.15
- removed net N$1689: J79.8, J81.24
- removed net N$1690: J79.7, J81.16
- removed net N$1691: J79.6, J81.17
- removed net N$1692: J79.68, J80.20
- removed net N$1693: J79.66, J80.16
- removed net N$1694: J79.64, J80.21
- removed net N$1695: J79.63, J80.14
- removed net N$1696: J79.62, J80.22
- removed net N$1697: J79.61, J80.23
- removed net N$1698: J79.60, J80.13
- removed net N$1699: J79.59, J80.24
- removed net N$1700: J79.58, J80.25
- removed net N$1701: J79.57, J80.12
- removed net N$1702: J79.56, J80.26
- removed net N$1703: J79.55, J80.11
- removed net N$1704: J79.54, J80.27
- removed net N$1705: J79.53, J80.10
- removed net N$1706: J79.52, J80.28
- removed net N$1707: J79.51, J80.9
- removed net N$1708: J79.50, J80.29
- removed net N$1709: J79.49, J80.8
- removed net N$1710: J79.48, J80.30
- removed net N$1711: J79.47, J80.31
- removed net N$1712: J79.46, J80.7
- removed net N$1713: J79.45, J80.32
- removed net N$1714: J79.44, J80.33
- removed net N$1715: J79.43, J80.6
- removed net N$1716: J79.42, J80.34
- removed net N$1717: J79.41, J80.35
- removed net N$1718: J79.40, J80.5
- removed net N$1719: J79.38, J80.3
- removed net N$1720: J79.5, J81.23
- removed net N$1721: J79.4, J81.22
- removed net N$1722: J79.3, J81.21
- removed net N$1723: J79.2, J81.20
- removed net N$1724: J79.65, J80.15
- removed net N$1725: J79.67, J80.17
- removed net N$1726: J79.39, J80.4
- removed net N$1727: J79.37, J80.2
- removed net N$1728: J79.33, J81.2
- removed net N$1729: J82.32, J84.35
- removed net N$1730: J82.31, J84.34
- removed net N$1731: J82.30, J84.33
- removed net N$1732: J82.29, J84.3
- removed net N$1733: J82.28, J84.32
- removed net N$1734: J82.27, J84.4
- removed net N$1735: J82.26, J84.5
- removed net N$1736: J82.25, J84.31
- removed net N$1737: J82.24, J84.6
- removed net N$1738: J82.23, J84.7
- removed net N$1739: J82.22, J84.30
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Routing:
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- added copper zone on layer 1, net S$1
- added copper zone on layer 1, net S$2
- added copper zone on layer 1, net S$3
- added copper zone on layer 1, net S$4
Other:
- board size 109 x 119 mm -> 119 x 83 mm
- board text added: "(5,10) mm"
- board text added: "(90,75) mm"
- board text added: "(94,12) mm"
- board text added: "JPN/Open Ephys"
- board text added: "OA-64, r1.0"
- board text added: "Thickness: 0.8 mm Color: Green"
- board text removed: "(6, 11)"
- board text removed: "(92, 97)"
- board text removed: "(94, 20)"
- board text removed: "OA-64 JPN"

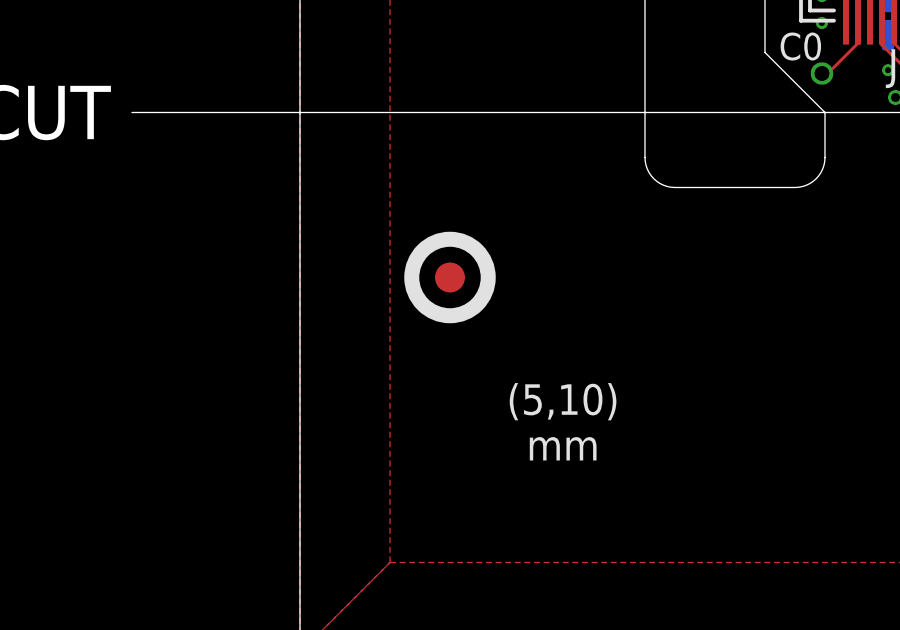
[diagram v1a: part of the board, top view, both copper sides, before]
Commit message: Fixed incorrect fiducial marker label on omnetics-adapter-64_panel
- It was labelled with the wrong coordinates
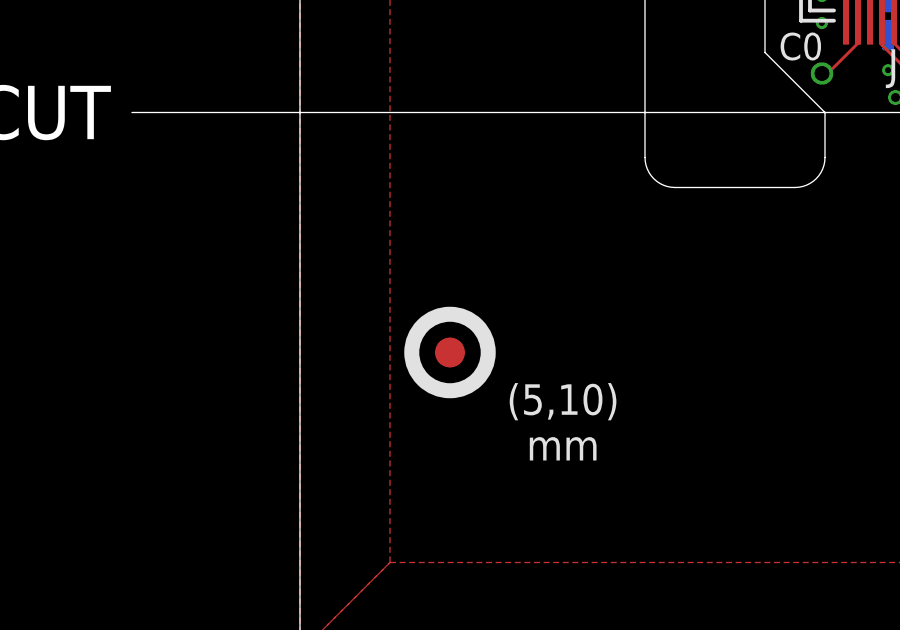
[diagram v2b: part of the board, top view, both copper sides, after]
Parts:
- moved E$1 2.50 mm to (5.00, 10.0)
